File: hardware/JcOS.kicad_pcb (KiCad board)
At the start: 2 copper layers, 65 x 56.5 mm, 6 parts, among them J1 Conn_01x04_Pin, J2 RPi_GPIO, SW1 SW_Push, U1 LCD-16X2

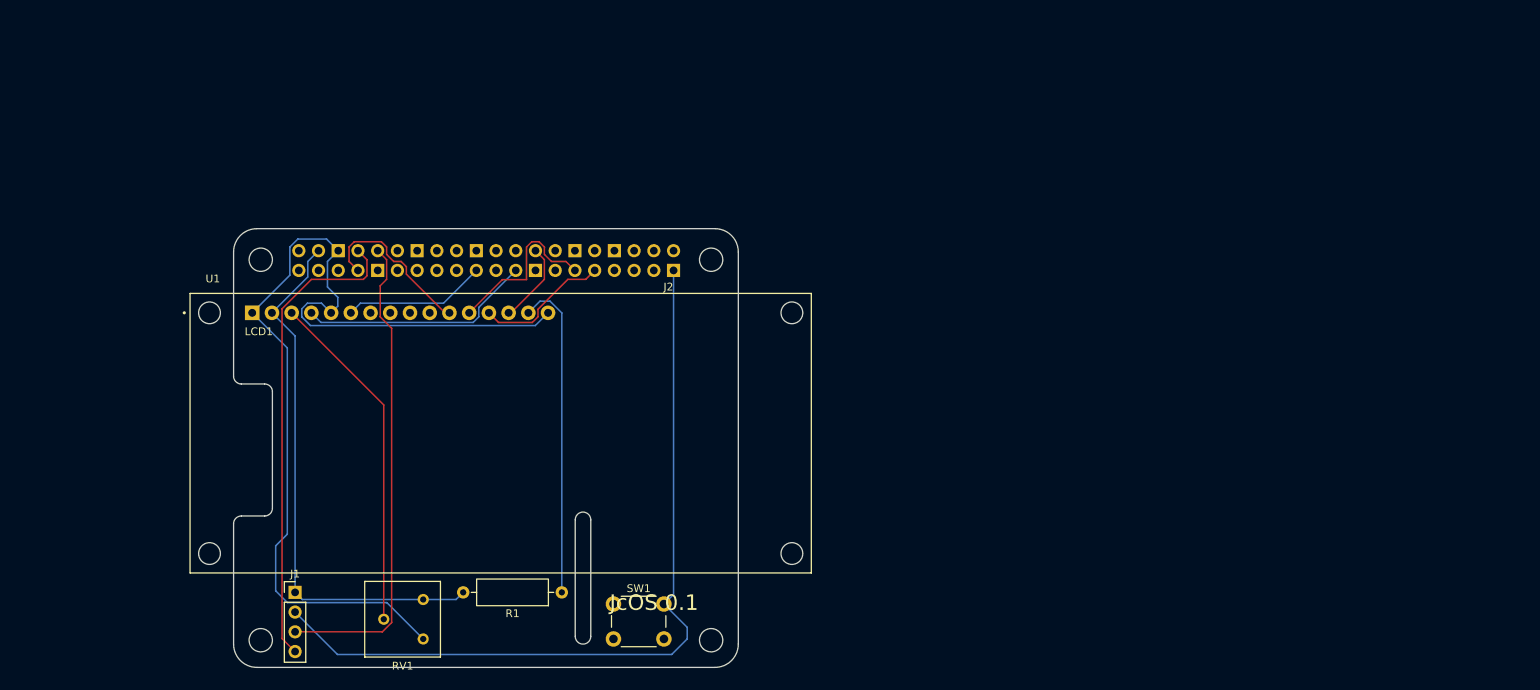
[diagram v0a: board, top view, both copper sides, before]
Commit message: feat: 3.5" SPI TFT LCD hat board
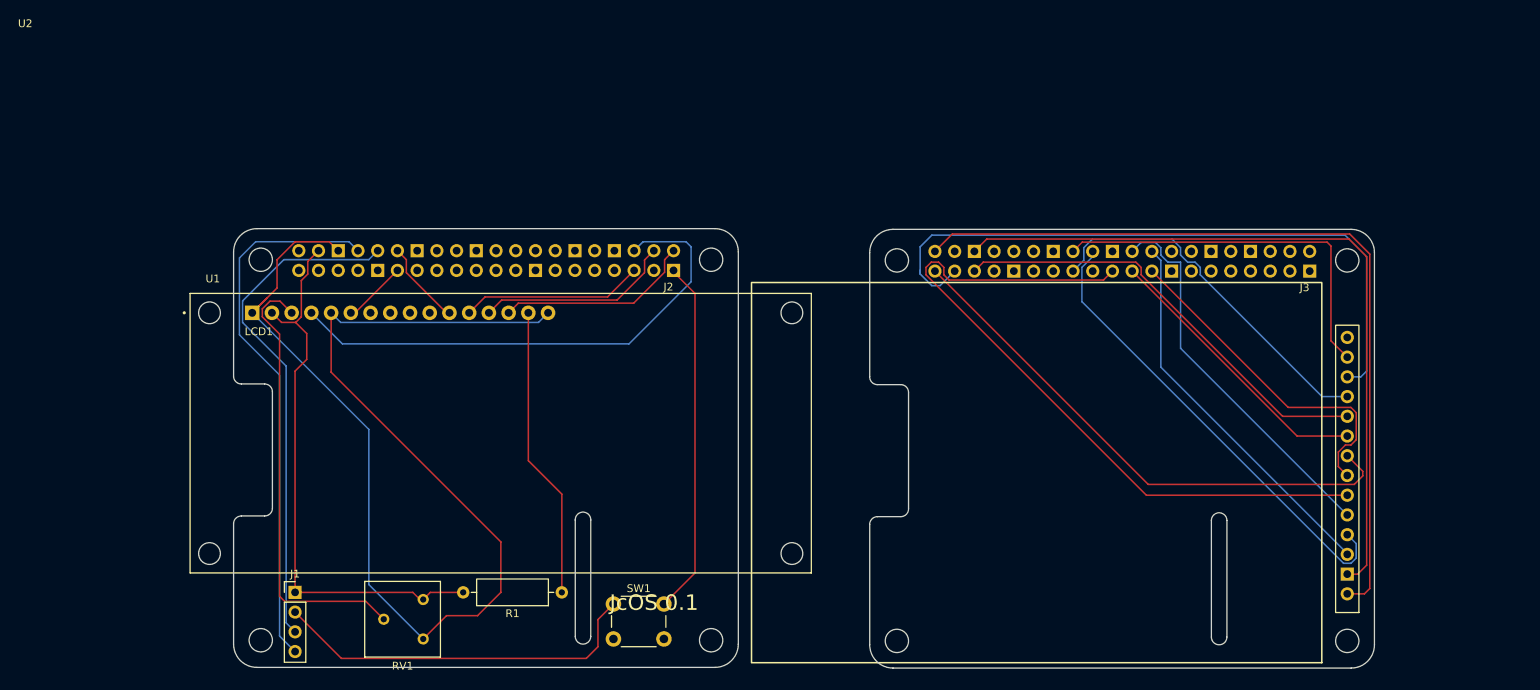
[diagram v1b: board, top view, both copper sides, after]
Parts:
- added J3: RPi_GPIO, RPI_Hat:RPI_Hat_B+, F.Cu at (141.5, 30.2)
- added U2: 3.5" TFT LCD, Display:3.5_ TFT LCD, F.Cu at (130.5, 57.6)
- added U2: ~, Display:3.5_ TFT LCD, F.Cu at (0.25, 0.25)
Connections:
- J2 pad 11: unconnected-(J2-BCM17-Pad11) -> Net-(J2-BCM17)
- J2 pad 12: unconnected-(J2-BCM18_PCM_C-Pad12) -> Net-(J2-BCM18_PCM_C)
- J2 pad 19: Net-(J2-BCM10_MOSI) -> unconnected-(J2-BCM10_MOSI-Pad19)
- J2 pad 23: Net-(J2-BCM11_SCLK) -> unconnected-(J2-BCM11_SCLK-Pad23)
- J2 pad 26: Net-(J2-BCM7_CE1) -> unconnected-(J2-BCM7_CE1-Pad26)
- J2 pad 29: Net-(J2-BCM5) -> unconnected-(J2-BCM5-Pad29)
- J2 pad 31: Net-(J2-BCM6) -> unconnected-(J2-BCM6-Pad31)
- J2 pad 35: unconnected-(J2-BCM19_MISO_PCM_FS-Pad35) -> Net-(J2-BCM19_MISO_PCM_FS)
- J2 pad 36: unconnected-(J2-BCM16-Pad36) -> Net-(J2-BCM16)
- J2 pad 38: unconnected-(J2-BCM20_MOSI_PCM_DI-Pad38) -> Net-(J2-BCM20_MOSI_PCM_DI)
- J2 pad 40: unconnected-(J2-BCM21_SCLK_PCM_DO-Pad40) -> Net-(J2-BCM21_SCLK_PCM_DO)
- J2 pad 7: Net-(J2-BCM4_GPCLK0) -> unconnected-(J2-BCM4_GPCLK0-Pad7)
- U1 pad 11: Net-(J2-BCM4_GPCLK0) -> Net-(J2-BCM18_PCM_C)
- U1 pad 12: Net-(J2-BCM5) -> Net-(J2-BCM19_MISO_PCM_FS)
- U1 pad 13: Net-(J2-BCM6) -> Net-(J2-BCM20_MOSI_PCM_DI)
- U1 pad 14: Net-(J2-BCM7_CE1) -> Net-(J2-BCM21_SCLK_PCM_DO)
- U1 pad 4: Net-(J2-BCM11_SCLK) -> Net-(J2-BCM16)
- U1 pad 6: Net-(J2-BCM10_MOSI) -> Net-(J2-BCM17)
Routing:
- net Net-(U2-VCC): track 0.00 -> 104.2 mm
- net Net-(U2-GND): track 0.00 -> 94.8 mm
- net Net-(J3-BCM10_MOSI): track 0.00 -> 93.2 mm
- net Net-(J3-BCM2_SDA): track 0.00 -> 86.6 mm
- net Net-(U2-LED): track 0.00 -> 70.4 mm
- net Net-(J2-BCM16): track 0.00 -> 66.5 mm
- net Net-(J3-BCM24): track 0.00 -> 60.1 mm
- net Net-(J3-BCM3_SCL): track 0.00 -> 57.3 mm
- net Net-(J3-BCM25): track 0.00 -> 49.8 mm
- net Net-(J3-BCM8_CE0): track 0.00 -> 49.4 mm
- net Net-(J3-BCM23): track 0.00 -> 49.1 mm
- net Net-(J3-BCM22): track 0.00 -> 47.5 mm
- net Net-(J3-BCM11_SCLK): track 0.00 -> 43.8 mm
- net Net-(J3-BCM9_MISO): track 0.00 -> 36.5 mm
- net Net-(U1-K): track 126.3 -> 157.8 mm
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
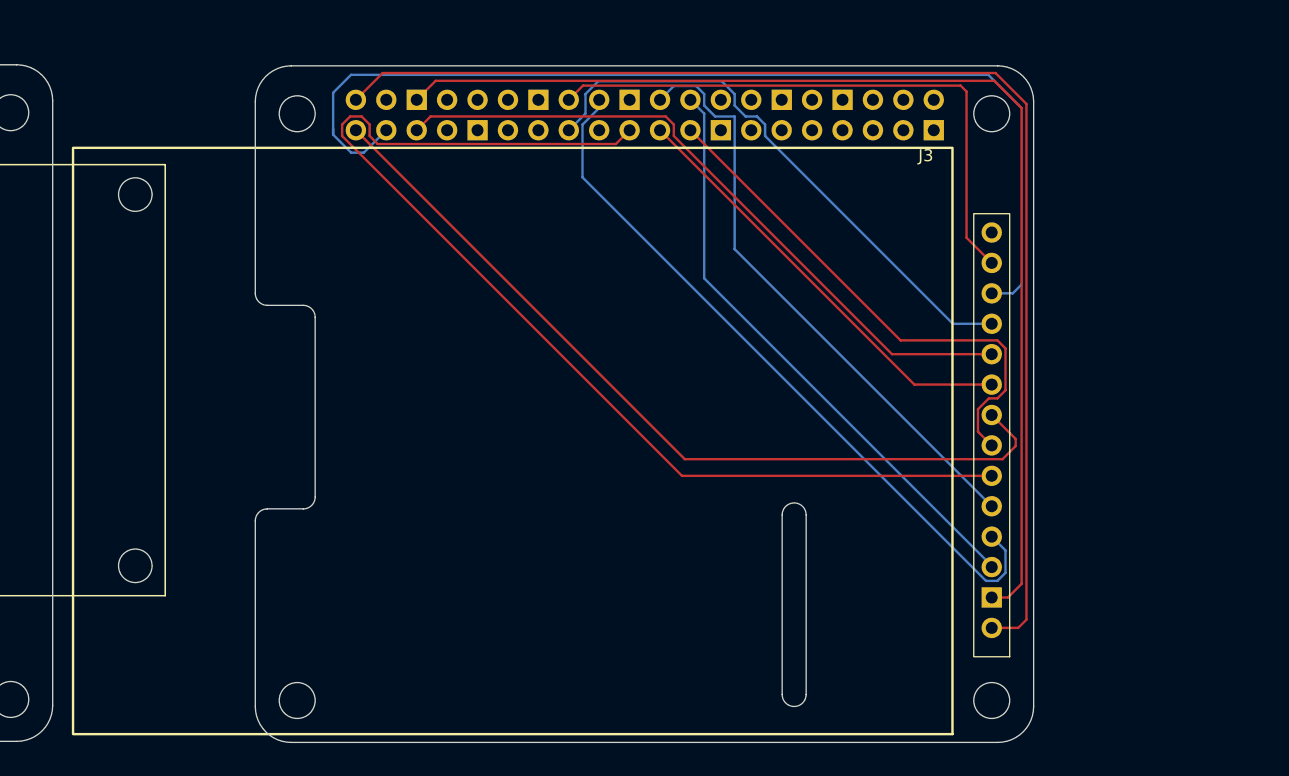
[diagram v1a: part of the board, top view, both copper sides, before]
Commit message: feat: reverse LCD PCB and add serial connector
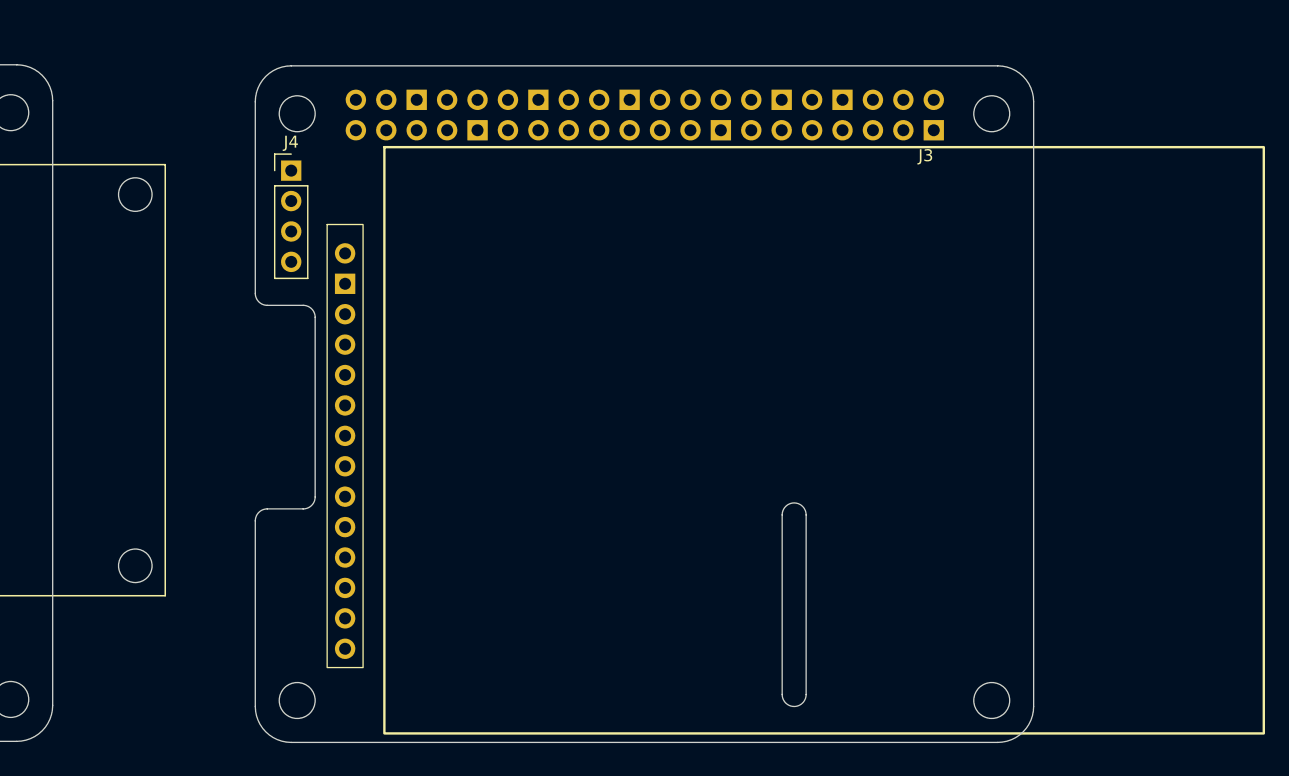
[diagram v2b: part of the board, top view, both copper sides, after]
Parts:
- added J4: Conn_01x04_Pin, Connector_PinHeader_2.54mm:PinHeader_1x04_P2.54mm_Vertical, F.Cu at (112.0, 35.0)
- moved U2 26.0 mm to (156.5, 57.5), turned to 0 degrees
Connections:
- J3 pad 10: unconnected-(J3-BCM15_RXD-Pad10) -> Net-(J3-BCM15_RXD)
- J3 pad 22: Net-(J3-BCM25) -> Net-(J3-BCM14_TXD)
- J3 pad 8: unconnected-(J3-BCM14_TXD-Pad8) -> Net-(J3-BCM14_TXD)
- U2 pad 5: Net-(J3-BCM25) -> Net-(J3-BCM14_TXD)
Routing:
- net Net-(U2-VCC): track 104.2 -> 0.00 mm
- net Net-(U2-GND): track 94.8 -> 0.00 mm
- net Net-(J3-BCM10_MOSI): track 93.2 -> 0.00 mm
- net Net-(J3-BCM2_SDA): track 86.6 -> 0.00 mm
- net Net-(U2-LED): track 70.4 -> 0.00 mm
- net Net-(J3-BCM24): track 60.1 -> 0.00 mm
- net Net-(J3-BCM3_SCL): track 57.3 -> 0.00 mm
- net Net-(J3-BCM25): track 49.8 -> 0.00 mm
- net Net-(J3-BCM8_CE0): track 49.4 -> 0.00 mm
- net Net-(J3-BCM23): track 49.1 -> 0.00 mm
- net Net-(J3-BCM22): track 47.5 -> 0.00 mm
- net Net-(J3-BCM11_SCLK): track 43.8 -> 0.00 mm
- net Net-(J3-BCM9_MISO): track 36.5 -> 0.00 mm

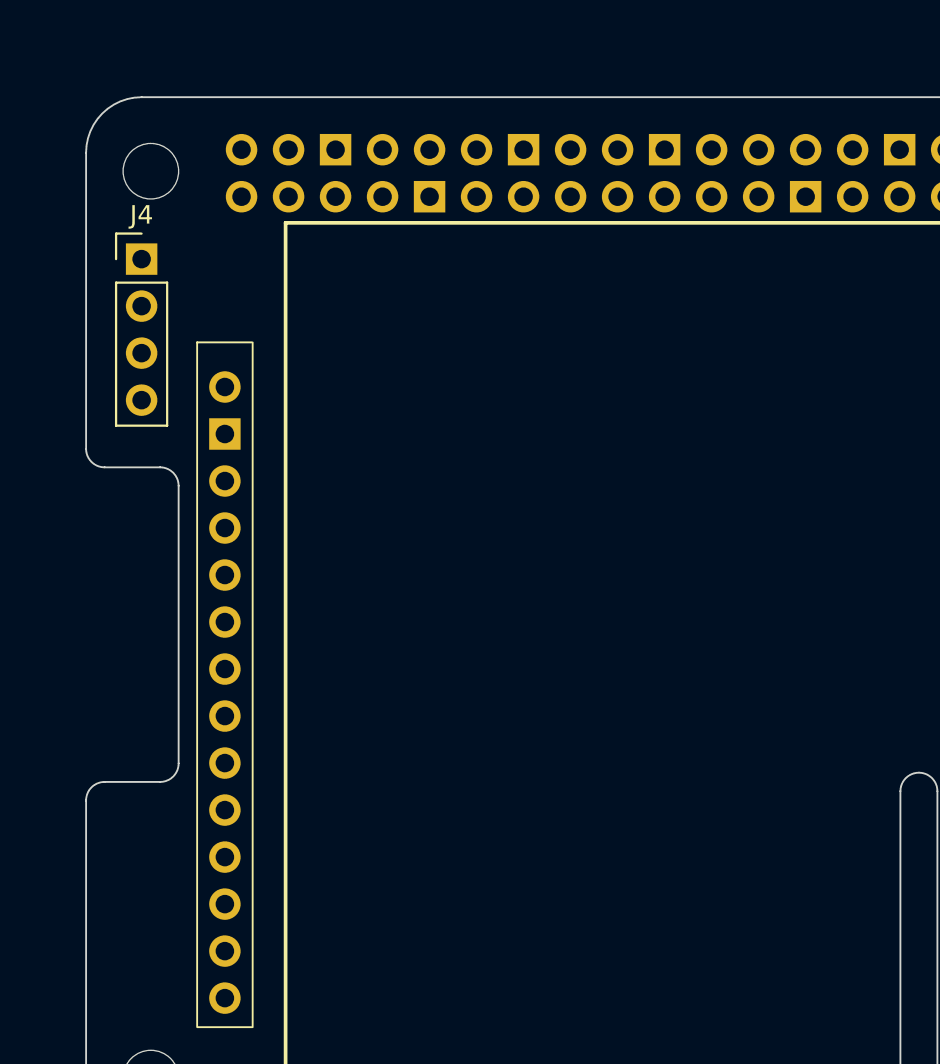
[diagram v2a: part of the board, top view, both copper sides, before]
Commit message: feat: wire up tft spi lcd
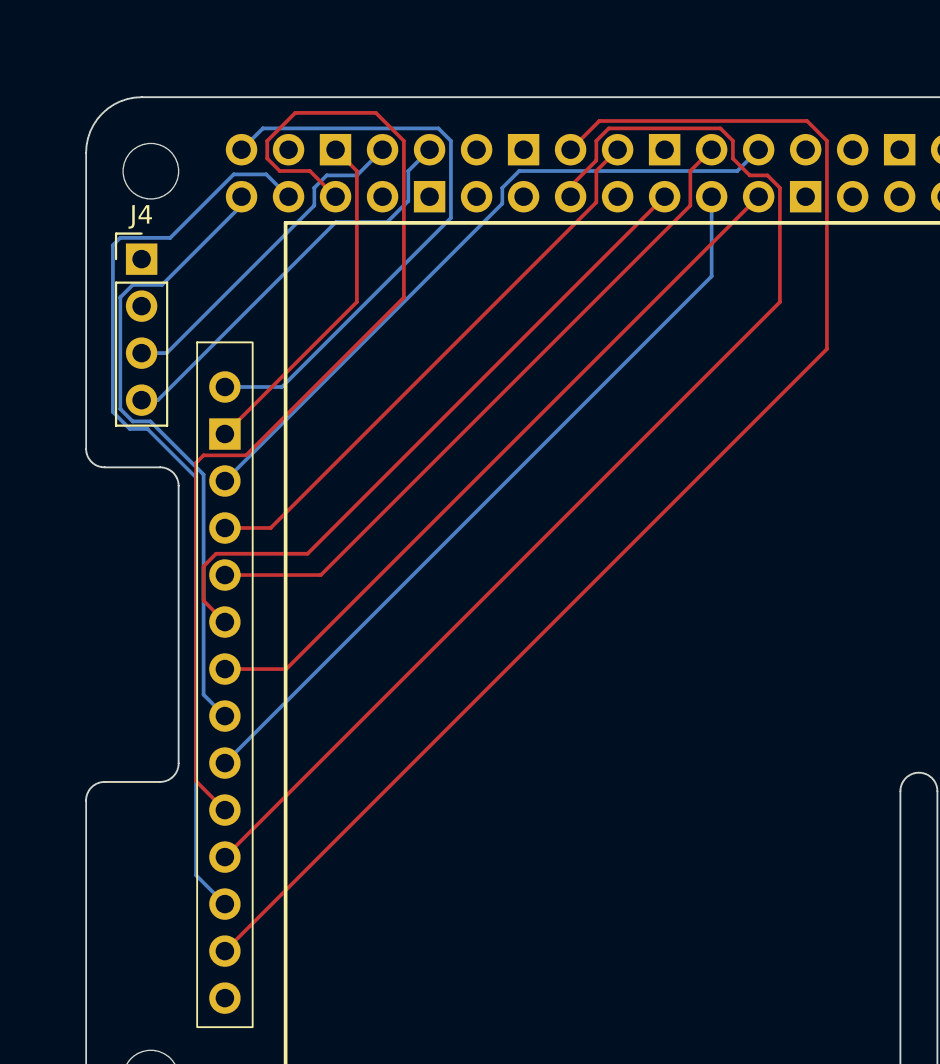
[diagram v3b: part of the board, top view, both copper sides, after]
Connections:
- J3 pad 14: unconnected-(J3-GND-Pad14) -> Net-(J4-Pin_1)
- J3 pad 22: Net-(J3-BCM14_TXD) -> Net-(J3-BCM25)
- J4 pad 1: Net-(J3-BCM14_TXD) -> Net-(J4-Pin_1)
- J4 pad 2: Net-(J3-BCM15_RXD) -> unconnected-(J4-Pin_2-Pad2)
- J4 pad 3: unconnected-(J4-Pin_3-Pad3) -> Net-(J3-BCM14_TXD)
- J4 pad 4: unconnected-(J4-Pin_4-Pad4) -> Net-(J3-BCM15_RXD)
- U2 pad 5: Net-(J3-BCM14_TXD) -> Net-(J3-BCM25)
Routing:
- net Net-(J3-BCM23): track 0.00 -> 72.2 mm
- net Net-(J3-BCM22): track 0.00 -> 64.3 mm
- net Net-(J3-BCM3_SCL): track 0.00 -> 56.9 mm
- net Net-(J3-BCM2_SDA): track 0.00 -> 50.2 mm
- net Net-(J3-BCM9_MISO): track 0.00 -> 41.5 mm
- net Net-(J3-BCM11_SCLK): track 0.00 -> 39.4 mm
- net Net-(J3-BCM25): track 0.00 -> 36.9 mm
- net Net-(J3-BCM8_CE0): track 0.00 -> 36.8 mm
- net Net-(J3-BCM10_MOSI): track 0.00 -> 36.7 mm
- net Net-(U2-LED): track 0.00 -> 34.6 mm
- net Net-(U2-VCC): track 0.00 -> 32.2 mm
- net Net-(J3-BCM24): track 0.00 -> 30.7 mm
- net Net-(J3-BCM15_RXD): track 0.00 -> 22.1 mm
- net Net-(U2-GND): track 0.00 -> 18.8 mm
- net Net-(J3-BCM14_TXD): track 0.00 -> 18.1 mm
